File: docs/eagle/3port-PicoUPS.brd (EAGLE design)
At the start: 57.2 x 64.8 mm, 44 parts, among them IC1 MAX471CPA, IC2 MAX471CPA, IC3 MAX471CPA, IC6 7805TV, U1 P012PTH

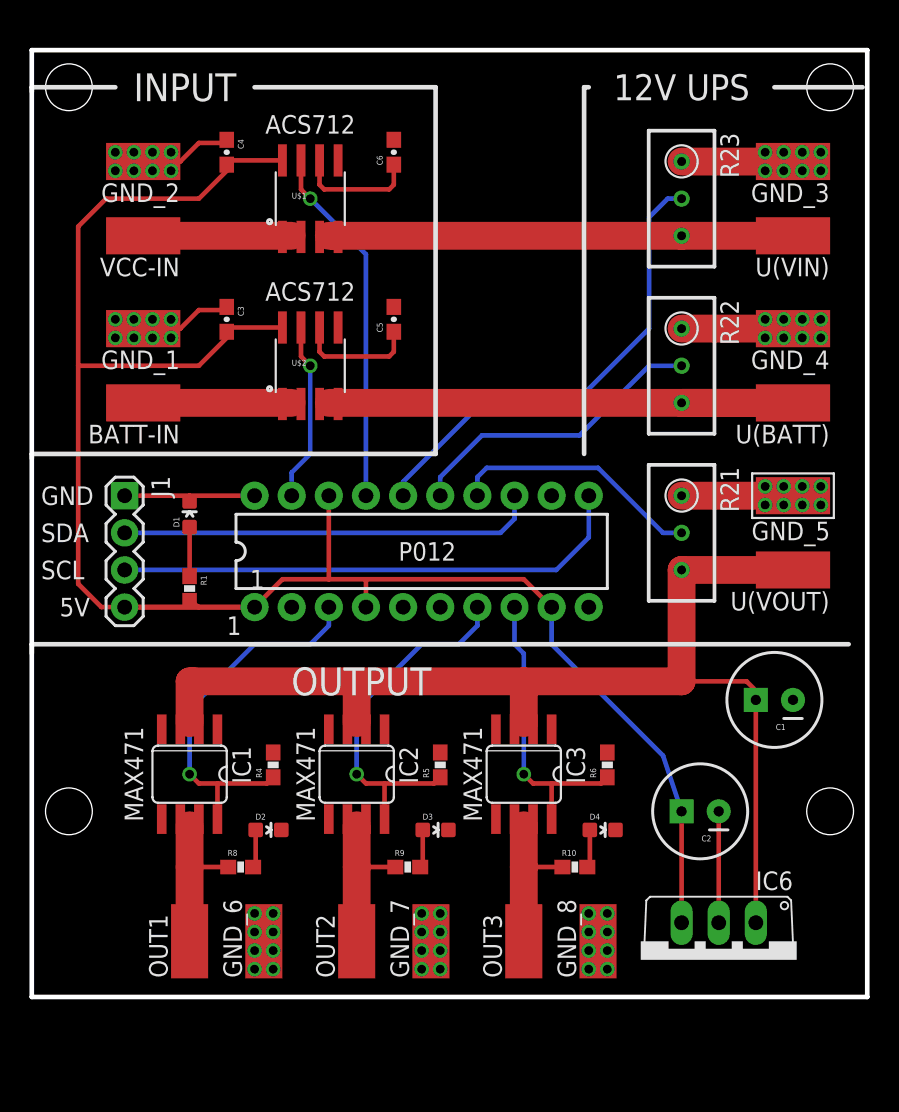
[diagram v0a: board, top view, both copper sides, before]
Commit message: Replaced 7805 with SMD LM1117 - moved it up the board in preparation of adding switches on the output ports
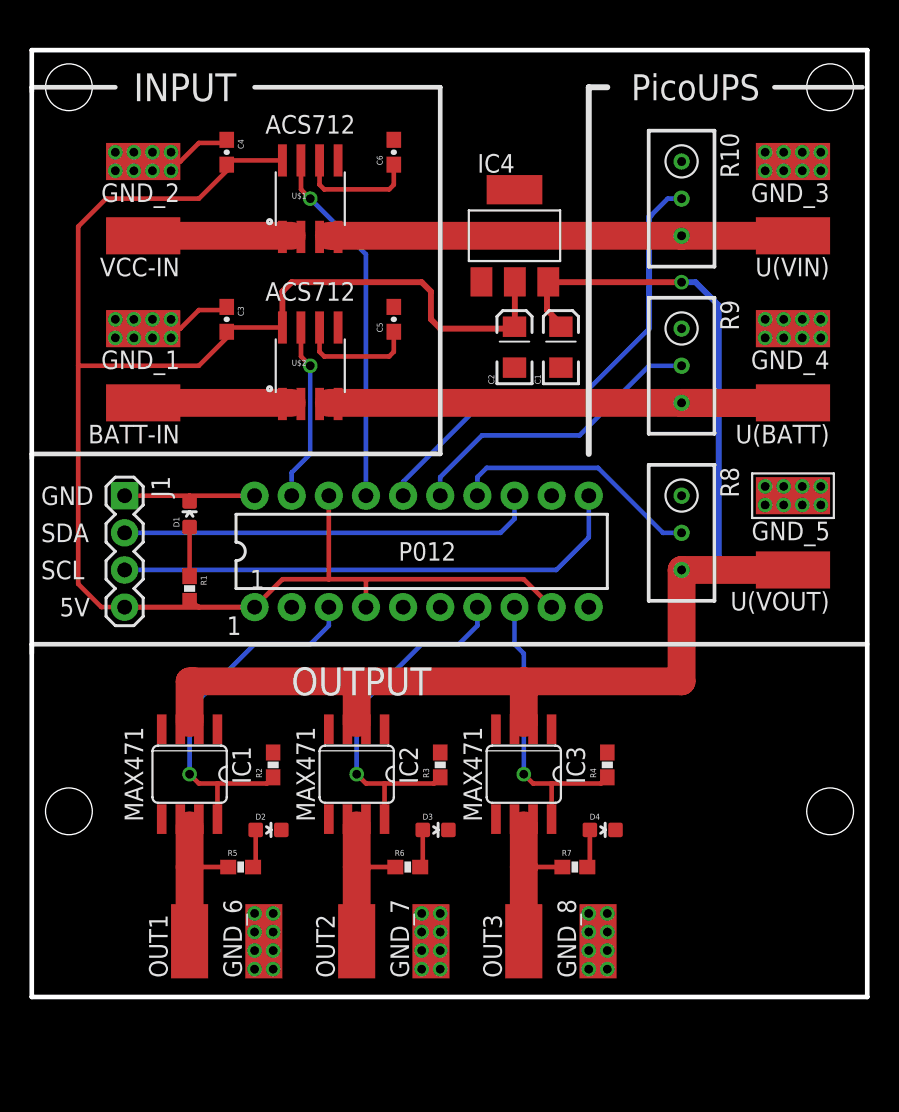
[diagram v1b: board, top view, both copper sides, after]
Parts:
- removed IC6: 7805TV, linear:TO220V
- removed R21, R22, R23: 10k, rcl:RTRIM3296W
- added IC4: REG1117, burr-brown:SOT223
- added R2, R3, R7: 1k, SparkFun-Passives:0603-RES
- C1: value 100uF -> 10uF; device SparkFun-Capacitors:CPOL-RADIAL-100UF-25V -> SparkFun-Capacitors:EIA3216
- C2: device SparkFun-Capacitors:CPOL-RADIAL-100UF-25V -> SparkFun-Capacitors:EIA3216
- R10, R8, R9: value 1k -> 10k; device SparkFun-Passives:0603-RES -> rcl:RTRIM3296W
- moved R10 46.3 mm to (40.6, 68.6), turned to 180 degrees
- moved R9 39.1 mm to (40.6, 57.1), turned to 180 degrees
- moved R8 37.8 mm to (40.6, 45.7), turned to 180 degrees
- moved C2 34.2 mm to (29.2, 58.4), turned to 90 degrees
- moved C1 28.2 mm to (32.4, 58.4), turned to 90 degrees
- moved R4 22.9 mm to (35.6, 29.8)
- moved R6 15.3 mm to (21.9, 22.9), turned to 0 degrees
- moved R5 15.3 mm to (10.5, 22.9), turned to 0 degrees
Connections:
- net 12V: now also C1.A, IC4.3, R8.3; no longer C1.1, IC6.1, R21.3
- net 5V: now also C2.A, IC4.2; no longer C2.1, IC6.3
- net BATT-UPS: now also R9.3; no longer R22.3
- net GND: now also C1.C, C2.C, IC4.1, R10.1, R2.2, R3.2, R8.1, R9.1; no longer C1.2, C2.2, IC6.2, R21.1, R22.1, R23.1, R5.2, R6.2
- net I1: now also R2.1; no longer R4.1
- net I2: now also R3.1; no longer R5.1
- net I3: now also R4.1; no longer R6.1
- net N$6: now also R5.2; no longer R8.2
- net N$7: now also R6.2; no longer R9.2
- net N$8: now also R7.2; no longer R10.2
- net OUT1: now also R5.1; no longer R8.1
- net OUT2: now also R6.1; no longer R9.1
- net OUT3: now also R7.1; no longer R10.1
- net V-BATT: now also R9.2; no longer R22.2
- net V-UPS: now also R8.2; no longer R21.2
- net V-VCC: now also R10.2; no longer R23.2
- net VCC-UPS: now also R10.3; no longer R23.3
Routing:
- net GND: track 56.9 -> 26.4 mm
- net 12V: track 87.3 -> 101.9 mm, vias 0 -> 1
- net 5V: track 133.1 -> 132.3 mm
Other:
- board text added: "PicoUPS"
- board text removed: "12V UPS"

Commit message: Upgraded Eagle to 8.2.2; named 'VCC' and 'BATT' signal lines
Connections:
- net N$10 renamed BATT
- net N$9 renamed VCC
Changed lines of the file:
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@@
 <?xml version="1.0" encoding="utf-8"?>
 <!DOCTYPE eagle SYSTEM "eagle.dtd">
-<eagle version="7.6.0">
+<eagle version="8.2.2">
 <drawing>
 <settings>
@@
 <element name="IC1" library="maxim" package="SO08" value="MAX471CPA" x="6.985" y="29.21" rot="R180">
 <attribute name="MF" value="" x="6.985" y="29.21" size="1.778" layer="27" rot="R180" display="off"/>
+<attribute name="MPN" value="" x="6.985" y="29.21" size="1.778" layer="27" rot="R180" display="off"/>
 <attribute name="OC_FARNELL" value="unknown" x="6.985" y="29.21" size="1.778" layer="27" rot="R180" display="off"/>
 <attribute name="OC_NEWARK" value="unknown" x="6.985" y="29.21" size="1.778" layer="27" rot="R180" display="off"/>
-<attribute name="MPN" value="" x="6.985" y="29.21" size="1.778" layer="27" rot="R180" display="off"/>
 </element>
 <element name="IC2" library="maxim" package="SO08" value="MAX471CPA" x="18.415" y="29.21" rot="R180">
 <attribute name="MF" value="" x="18.415" y="29.21" size="1.778" layer="27" rot="R180" display="off"/>
+<attribute name="MPN" value="" x="18.415" y="29.21" size="1.778" layer="27" rot="R180" display="off"/>
 <attribute name="OC_FARNELL" value="unknown" x="18.415" y="29.21" size="1.778" layer="27" rot="R180" display="off"/>
 <attribute name="OC_NEWARK" value="unknown" x="18.415" y="29.21" size="1.778" layer="27" rot="R180" display="off"/>
-<attribute name="MPN" value="" x="18.415" y="29.21" size="1.778" layer="27" rot="R180" display="off"/>
 </element>
 <element name="IC3" library="maxim" package="SO08" value="MAX471CPA" x="29.845" y="29.21" rot="R180">
 <attribute name="MF" value="" x="29.845" y="29.21" size="1.778" layer="27" rot="R180" display="off"/>
+<attribute name="MPN" value="" x="29.845" y="29.21" size="1.778" layer="27" rot="R180" display="off"/>
 <attribute name="OC_FARNELL" value="unknown" x="29.845" y="29.21" size="1.778" layer="27" rot="R180" display="off"/>
 <attribute name="OC_NEWARK" value="unknown" x="29.845" y="29.21" size="1.778" layer="27" rot="R180" display="off"/>
-<attribute name="MPN" value="" x="29.845" y="29.21" size="1.778" layer="27" rot="R180" display="off"/>
 </element>
 <element name="R1" library="SparkFun-Passives" package="0603-RES" value="1k" x="6.985" y="41.91" rot="R270"/>
@@
 </element>
 <element name="IC4" library="burr-brown" package="SOT223" value="REG1117" x="29.21" y="66.04">
-<attribute name="OC_FARNELL" value="1097566" x="29.21" y="66.04" size="1.778" layer="27" display="off"/>
 <attribute name="MF" value="" x="29.21" y="66.04" size="1.778" layer="27" display="off"/>
 <attribute name="MPN" value="REG1117" x="29.21" y="66.04" size="1.778" layer="27" display="off"/>
+<attribute name="OC_FARNELL" value="1097566" x="29.21" y="66.04" size="1.778" layer="27" display="off"/>
 <attribute name="OC_NEWARK" value="14P6981" x="29.21" y="66.04" size="1.778" layer="27" display="off"/>
 </element>
@@
 <wire x1="17.0688" y1="66.04" x2="16.8275" y2="66.04" width="0.3175" layer="1"/>
 </signal>
-<signal name="N$9">
+<signal name="VCC">
 <contactref element="VCC-IN" pad="1"/>
 <contactref element="U$1" pad="1"/>
@@
 <wire x1="14.605" y1="66.04" x2="13.97" y2="66.04" width="0.3175" layer="1"/>
 </signal>
-<signal name="N$10">
+<signal name="BATT">
 <contactref element="BATT-IN" pad="1"/>
 <contactref element="U$2" pad="1"/>

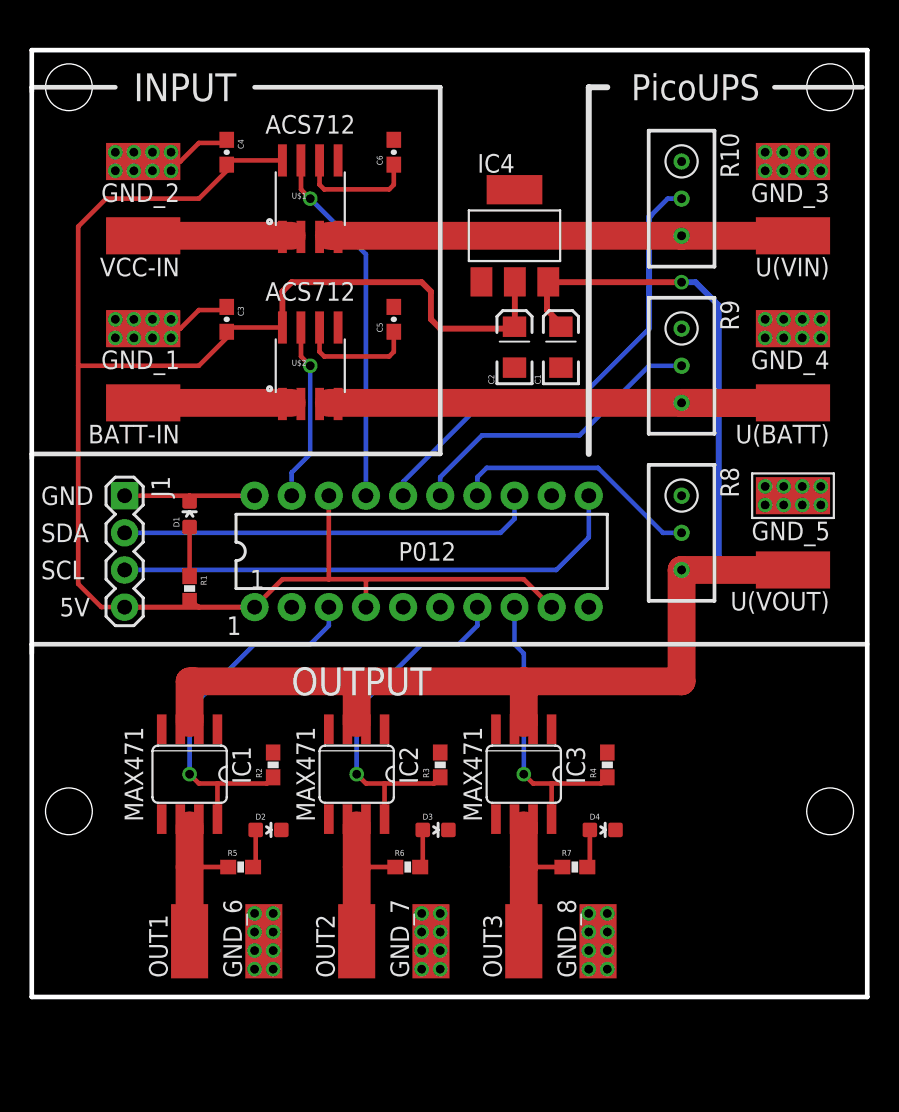
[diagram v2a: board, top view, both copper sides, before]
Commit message: Redesign the output section to include the relays and drivers.
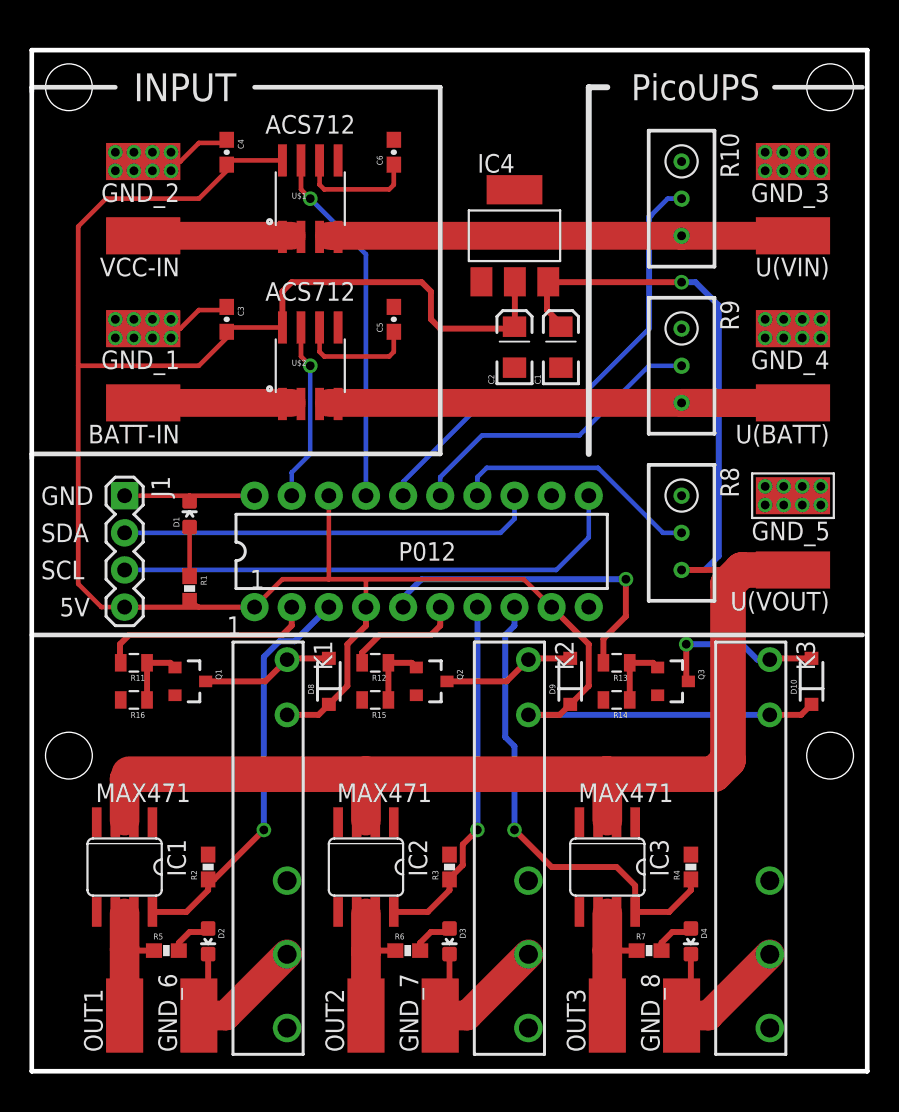
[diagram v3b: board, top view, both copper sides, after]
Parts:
- added D10, D8, D9: (no value), SparkFun-DiscreteSemi:SOD-123
- added K1, K2, K3: APF30212C, relay:APF30212C
- added Q1, Q2, Q3: MMBT2222A, SparkFun-DiscreteSemi:SOT23-3
- added R11, R12, R13: 1k, SparkFun-Passives:0805
- added R14, R15, R16: 10k, SparkFun-Passives:0805
- moved D4 9.72 mm to (41.3, 17.8), turned to 180 degrees
- moved R4 9.03 mm to (41.3, 22.9)
- moved D2 8.67 mm to (8.26, 17.8), turned to 180 degrees
- moved IC3 8.54 mm to (35.6, 22.9)
- moved R2 8.28 mm to (8.26, 22.9)
- moved IC1 7.75 mm to (2.54, 22.9)
- moved D3 7.68 mm to (24.8, 17.8), turned to 180 degrees
- moved GND_8 7.65 mm to (40.6, 12.7)
- moved OUT3 7.65 mm to (35.6, 12.7)
- moved R5 7.65 mm to (5.40, 17.1)
- moved R7 7.65 mm to (38.4, 17.1)
- moved R3 7.01 mm to (24.8, 22.9)
- moved OUT1 6.75 mm to (2.54, 12.7)
- moved GND_6 6.75 mm to (7.62, 12.7)
- moved IC2 6.38 mm to (19.1, 22.9)
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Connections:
- new net EN1: R11.2, U1.2
- new net EN2: R12.2, U1.6
- new net EN3: R13.2, U1.5
- new net GND_6: D2.C, GND_6.1, K1.COM
- new net GND_7: D3.C, GND_7.1, K2.COM
- new net GND_8: D4.C, GND_8.1, K3.COM
- new net N$10: D10.A, K3.1, Q3.3
- new net N$11: Q1.1, R11.1, R16.1
- new net N$13: Q2.1, R12.1, R15.1
- new net N$14: Q3.1, R13.1, R14.1
- new net N$5: D8.A, K1.1, Q1.3
- new net N$9: D9.A, K2.1, Q2.3
- net 5V: now also D10.C, D8.C, D9.C, K1.2, K2.2, K3.2
- net GND: now also K1.NC, K2.NC, K3.NC, Q1.2, Q2.2, Q3.2, R14.2, R15.2, R16.2; no longer D2.C, D3.C, D4.C, GND_6.1, GND_7.1, GND_8.1
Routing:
- net 5V: track 132.3 -> 174.4 mm
- net EN3: track 0.00 -> 22.8 mm, vias 0 -> 1
- net EN1: track 0.00 -> 14.8 mm
- net 12V: track 101.9 -> 115.6 mm
- net I3: track 20.3 -> 32.6 mm
- net GND_7: track 0.00 -> 12.2 mm
- net GND_6: track 0.00 -> 12.2 mm
- net GND_8: track 0.00 -> 12.2 mm
- net N$10: track 0.00 -> 11.6 mm, vias 0 -> 1
- net N$9: track 0.00 -> 9.14 mm
- net N$5: track 0.00 -> 9.09 mm
- net EN2: track 0.00 -> 8.07 mm
- net N$14: track 0.00 -> 4.58 mm
- net N$13: track 0.00 -> 4.58 mm
- net N$11: track 0.00 -> 4.58 mm
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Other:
- board size 57.2 x 64.8 mm -> 57.2 x 69.8 mm
- board text removed: "OUTPUT"

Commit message: Move from 0603 to 0805 components
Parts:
- C3, C4, C5, C6: device SparkFun-Capacitors:0603-CAP -> SparkFun-Capacitors:0805
- R1, R2, R3, R4, R5, R6, R7: device SparkFun-Passives:0603-RES -> SparkFun-Passives:0805
- R17, R19, R21: value 1k -> 390R
- moved C5 11.4 mm to (21.0, 71.8)
- moved C6 11.4 mm to (21.0, 60.3)
- moved R3 2.62 mm to (24.1, 25.4), turned to 270 degrees
- moved R2 2.62 mm to (7.62, 25.4), turned to 270 degrees
- moved R4 2.62 mm to (40.6, 25.4), turned to 270 degrees
- moved C4 1.27 mm to (9.53, 73.0)
- moved C3 1.27 mm to (9.53, 61.6)
- moved R1 0.95 mm to (6.99, 42.9)
- turned R20 to 0 degrees
- turned R5 to 180 degrees
- turned R6 to 180 degrees
- turned R7 to 180 degrees
- renumbered R11 to R21, R12 to R19, R13 to R17, R14 to R18, R15 to R20, R16 to R22
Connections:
- removed net N$6: D2.A, R5.2
- removed net N$7: D3.A, R6.2
- removed net N$8: D4.A, R7.2
- new net N$2: D2.A, R5.1
- new net N$3: D3.A, R6.1
- new net N$4: D4.A, R7.1
- net GND: now also R2.1, R20.1, R3.1, R4.1; no longer R2.2, R20.2, R3.2, R4.2
- net I1: now also R2.2; no longer R2.1
- net I2: now also R3.2; no longer R3.1
- net I3: now also R4.2; no longer R4.1
- net N$12: now also C5.1; no longer C6.1
- net N$13: now also R20.2; no longer R20.1
- net N$15: now also C6.1; no longer C5.1
- net OUT1: now also R5.2; no longer R5.1
- net OUT2: now also R6.2; no longer R6.1
- net OUT3: now also R7.2; no longer R7.1
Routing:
- net GND: track 24.6 -> 17.0 mm
- net 5V: track 174.4 -> 169.0 mm
- net N$6: track 2.95 -> 0.00 mm
- net N$8: track 2.95 -> 0.00 mm
- net N$7: track 2.95 -> 0.00 mm
- net N$2: track 0.00 -> 2.80 mm
- net N$3: track 0.00 -> 2.80 mm
- net N$4: track 0.00 -> 2.80 mm
- net I3: track 32.6 -> 34.2 mm
- net I1: track 28.1 -> 29.3 mm
- net N$1: track 3.35 -> 2.35 mm
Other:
- board text added: "pim@ipng.nl Version 1.2 github.com/pimvanpelt"
- board text removed: "pim@ipng.nl Version 1.1 github.com/pimvanpelt"
